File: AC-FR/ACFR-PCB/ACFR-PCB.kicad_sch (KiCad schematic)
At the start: 59 parts, among them J1 USB4105-GF-A, J2 Micro_SD_Card_Det1, J3 JST-SM04B-SRSS, J4 JST-PH, Q1 DMP2045U-7, Q2 DMP2045U-7, SW1 PTS636 SK25F, SW2 PTS636 SK25F, U1 ESP32-S3R8, U2 BMP390, U3 W25Q128JVPIQ, U4 W25Q128JVPIQ, U5 LSM6DSO32, U6 H3LIS331DLTR, U7 NCP187AMT330TAG, U8 LIS3MDL, Y1 ECS-400-8-36B-7KY

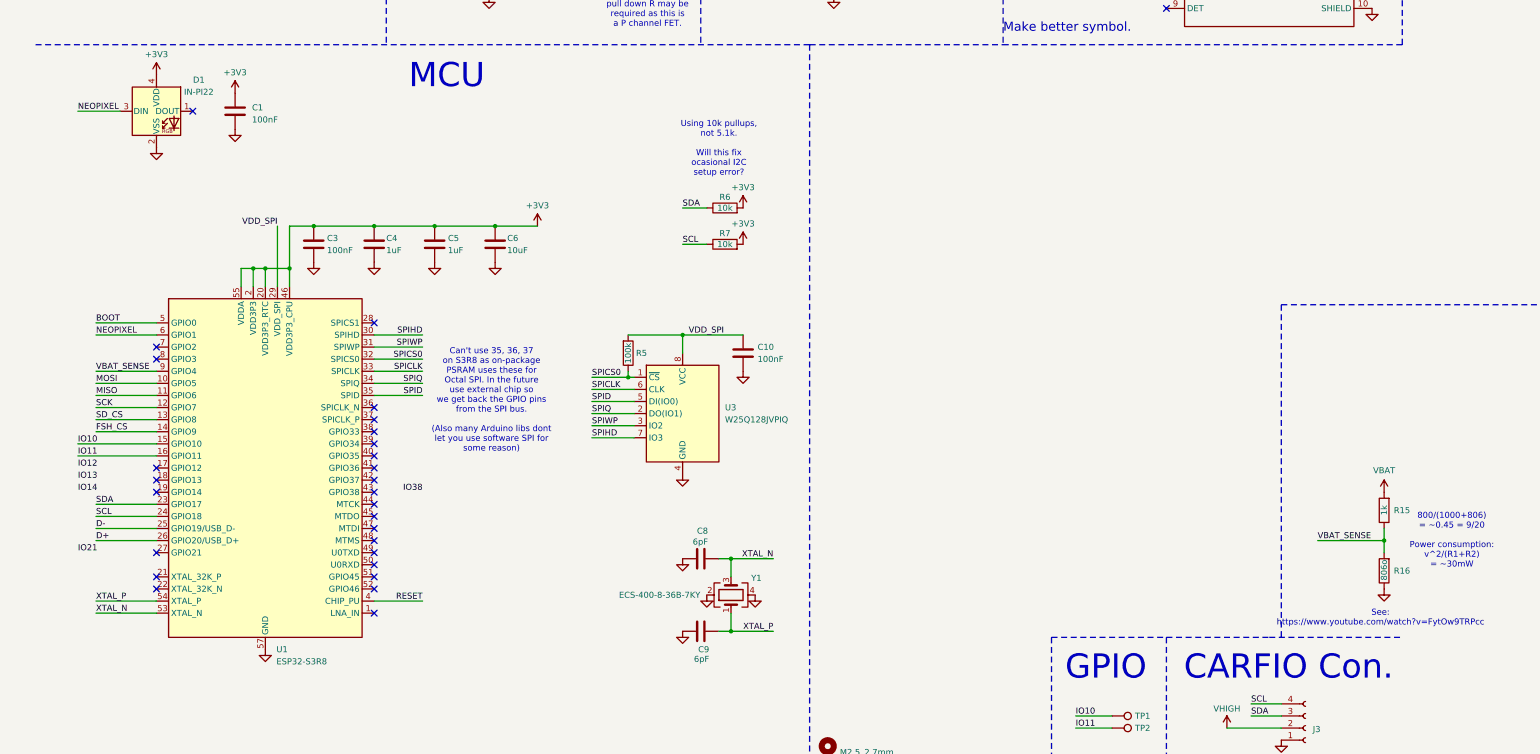
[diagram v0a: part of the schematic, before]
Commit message: why do the colors not not stay after a crash this was supposed to be fixed in fucking 8.0.2
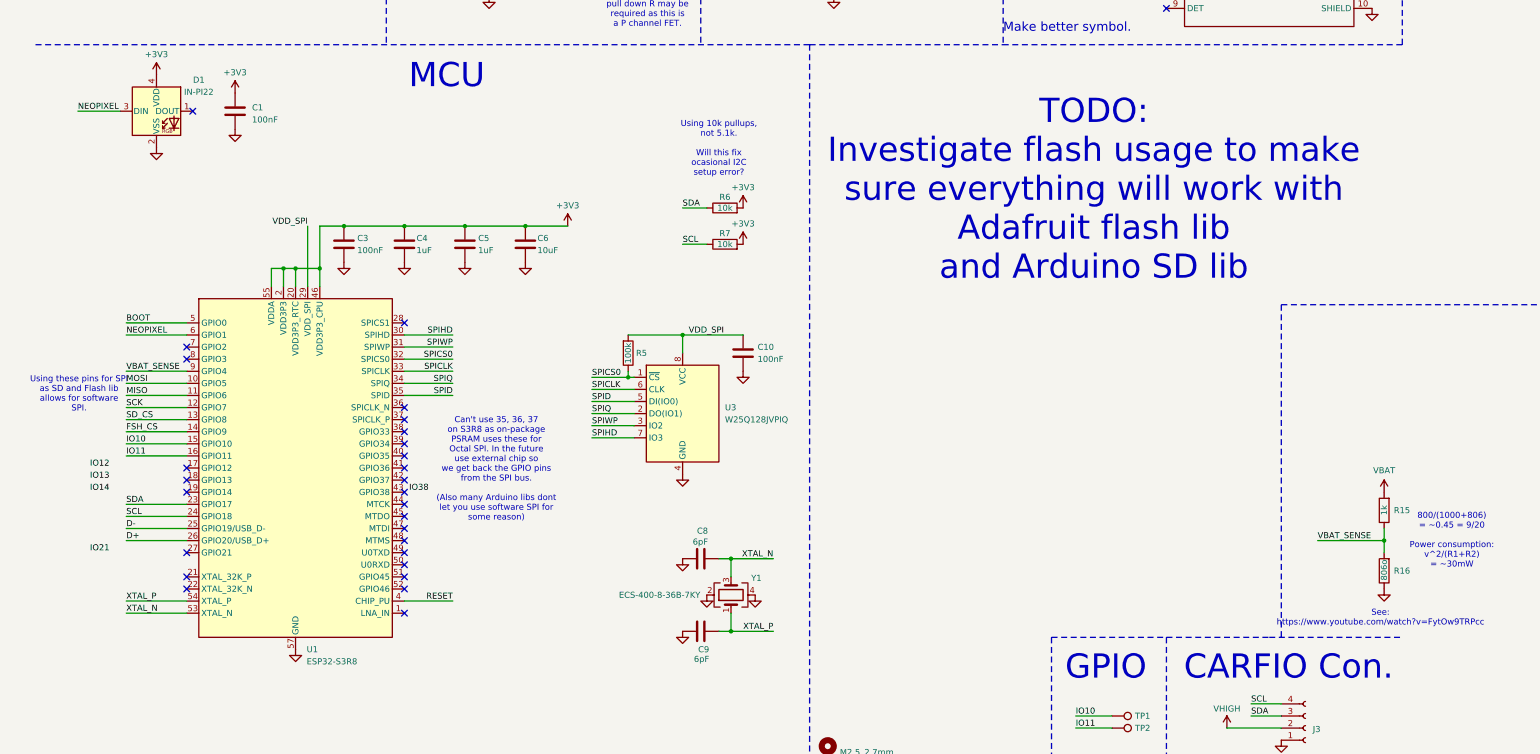
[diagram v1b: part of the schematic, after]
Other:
- note added: "TODO: Investigate flash usage to make sure everything will work with Adafruit flash lib and Arduino SD lib"
- note added: "Using these pins for SPI as SD and Flash lib allows for software SPI."
- moved on the sheet: C3, C4, C5, C6, U1

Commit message: Start on routing (kill the project, its horrible)
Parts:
- removed J3: JST-SM04B-SRSS, besser_footprints:JST_SH_SM04B-SRSS-TB_1x04-1MP_P1.00mm_Horizontal, symbol Connector:Conn_01x04_Socket
- added R8: 47k, Capacitor_SMD:C_0603_1608Metric, symbol Device:R
- renumbered C17 to C16, C18 to C17, C16 to C18, R9 to R10, R10 to R11, R11 to R12, R12 to R13, R13 to R14, R14 to R17, R8 to R9, U8 to U7, U7 to U8
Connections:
- net +3V3: now also R8.2
- net FSH_CS: now also R8.1
- net MISO: now also U1.13 (GPIO8); no longer U1.11 (GPIO6)
- net SD_CS: now also U1.11 (GPIO6); no longer U1.13 (GPIO8)
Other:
- note removed: "CARFIO Con."
- moved on the sheet: TP1, TP2
